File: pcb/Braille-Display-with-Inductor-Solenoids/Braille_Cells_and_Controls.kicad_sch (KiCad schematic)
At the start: 6 parts, among them U26 74HC595, U27 74HC595, U28 74HC595, U29 74HC595, U30 74HC595, U31 74HC595

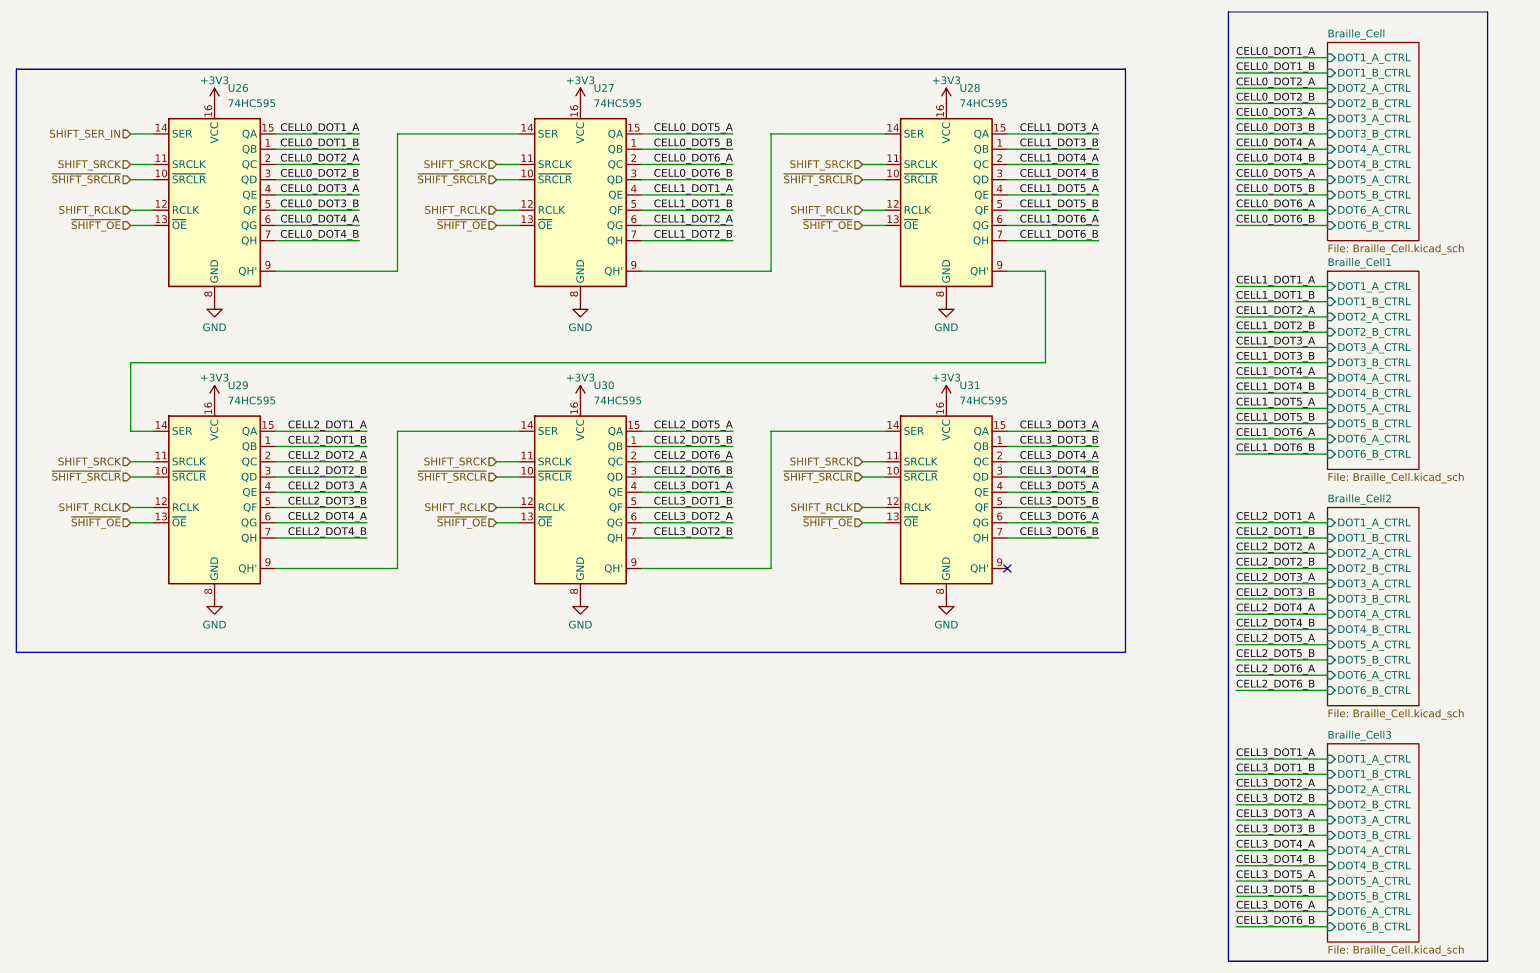
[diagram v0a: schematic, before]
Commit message: PCB (Rev 3): Switch to 2 inductors per cell (#2)
* WIP (Rev3): Switch to 2 inductors per cell

* WIP: Route one cell

* WIP: Route more of the board

* WIP: Swap around power input placement

* Finish and polish design

* Bit of tiny routing, export production file
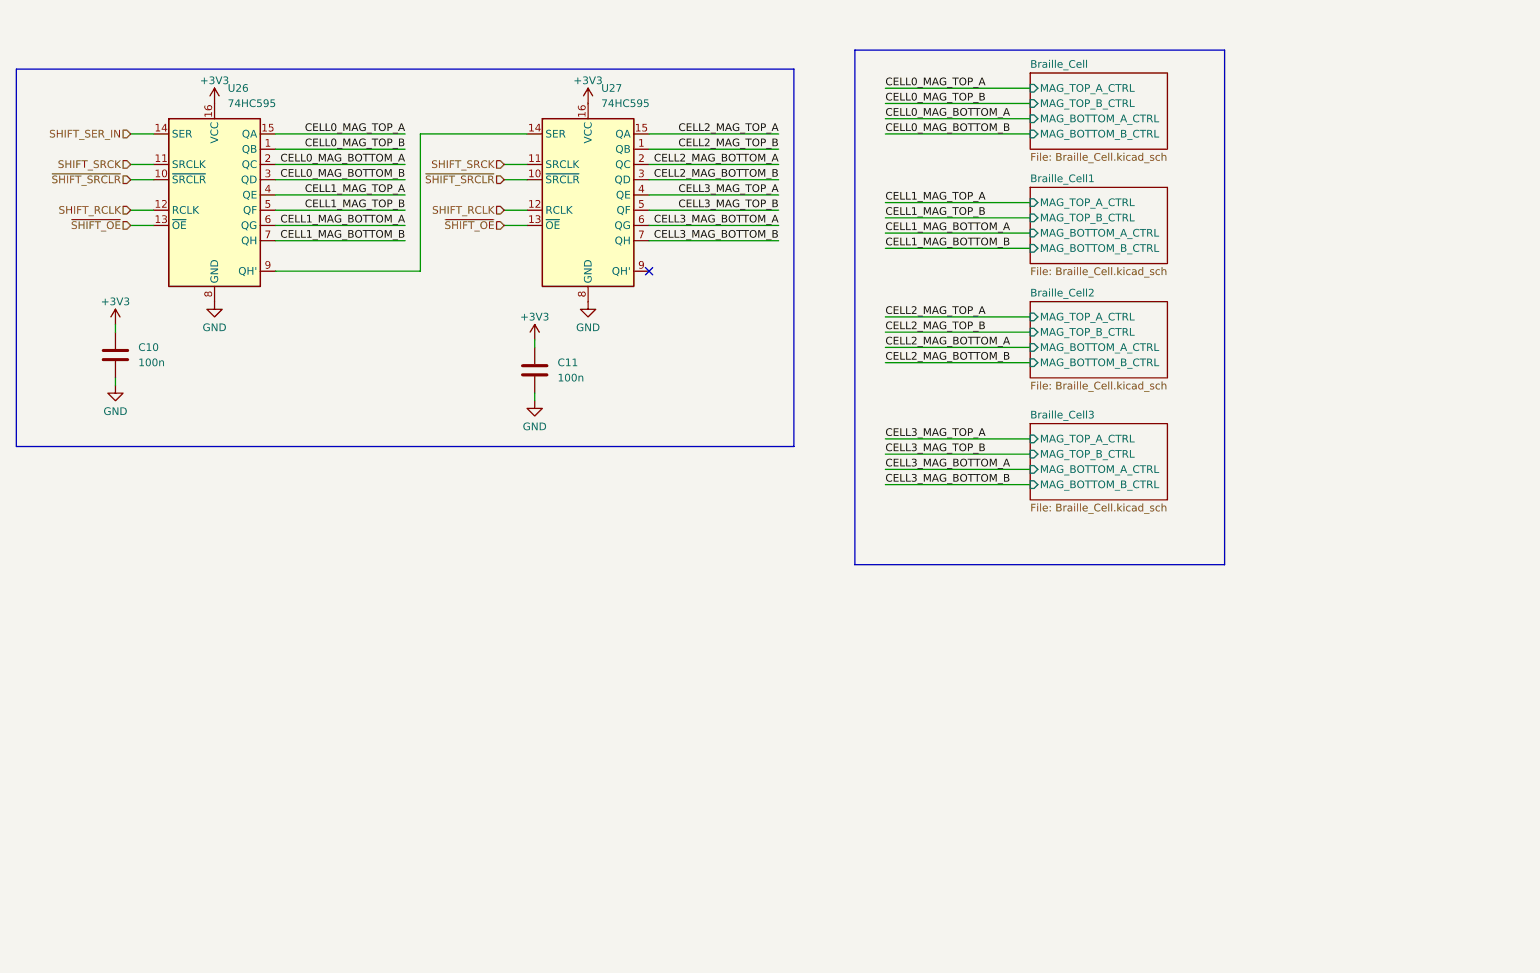
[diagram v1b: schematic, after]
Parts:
- removed U28, U29, U30, U31: 74HC595, Package_SO:SOP-16_3.9x9.9mm_P1.27mm, symbol 74xx:74HC595
- added C10, C11: 100n, Capacitor_SMD:C_1206_3216Metric_Pad1.33x1.80mm_HandSolder, symbol Device:C
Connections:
- net +3V3: now also C10.1, C11.1
- net GND: now also C10.2, C11.2
- net CELL0_DOT1_A renamed CELL0_MAG_TOP_A
- net CELL0_DOT1_B renamed CELL0_MAG_TOP_B
- net CELL0_DOT2_A renamed CELL0_MAG_BOTTOM_A
- net CELL0_DOT2_B renamed CELL0_MAG_BOTTOM_B
- net CELL0_DOT3_A renamed CELL1_MAG_TOP_A
- net CELL0_DOT3_B renamed CELL1_MAG_TOP_B
- net CELL0_DOT4_A renamed CELL1_MAG_BOTTOM_A
- net CELL0_DOT4_B renamed CELL1_MAG_BOTTOM_B
- net CELL0_DOT5_A renamed CELL2_MAG_TOP_A
- net CELL0_DOT5_B renamed CELL2_MAG_TOP_B
- net CELL0_DOT6_A renamed CELL2_MAG_BOTTOM_A
- net CELL0_DOT6_B renamed CELL2_MAG_BOTTOM_B
- net CELL1_DOT1_A renamed CELL3_MAG_TOP_A
- net CELL1_DOT1_B renamed CELL3_MAG_TOP_B
- net CELL1_DOT2_A renamed CELL3_MAG_BOTTOM_A
- net CELL1_DOT2_B renamed CELL3_MAG_BOTTOM_B
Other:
- sheet Braille_Cell ports: added MAG_BOTTOM_A_CTRL, MAG_BOTTOM_B_CTRL, MAG_TOP_A_CTRL, MAG_TOP_B_CTRL; removed DOT1_A_CTRL, DOT1_B_CTRL, DOT2_A_CTRL, DOT2_B_CTRL, DOT3_A_CTRL, DOT3_B_CTRL, DOT4_A_CTRL, DOT4_B_CTRL, DOT5_A_CTRL, DOT5_B_CTRL, DOT6_A_CTRL, DOT6_B_CTRL
- sheet Braille_Cell1 ports: added MAG_BOTTOM_A_CTRL, MAG_BOTTOM_B_CTRL, MAG_TOP_A_CTRL, MAG_TOP_B_CTRL; removed DOT1_A_CTRL, DOT1_B_CTRL, DOT2_A_CTRL, DOT2_B_CTRL, DOT3_A_CTRL, DOT3_B_CTRL, DOT4_A_CTRL, DOT4_B_CTRL, DOT5_A_CTRL, DOT5_B_CTRL, DOT6_A_CTRL, DOT6_B_CTRL
- sheet Braille_Cell2 ports: added MAG_BOTTOM_A_CTRL, MAG_BOTTOM_B_CTRL, MAG_TOP_A_CTRL, MAG_TOP_B_CTRL; removed DOT1_A_CTRL, DOT1_B_CTRL, DOT2_A_CTRL, DOT2_B_CTRL, DOT3_A_CTRL, DOT3_B_CTRL, DOT4_A_CTRL, DOT4_B_CTRL, DOT5_A_CTRL, DOT5_B_CTRL, DOT6_A_CTRL, DOT6_B_CTRL
- sheet Braille_Cell3 ports: added MAG_BOTTOM_A_CTRL, MAG_BOTTOM_B_CTRL, MAG_TOP_A_CTRL, MAG_TOP_B_CTRL; removed DOT1_A_CTRL, DOT1_B_CTRL, DOT2_A_CTRL, DOT2_B_CTRL, DOT3_A_CTRL, DOT3_B_CTRL, DOT4_A_CTRL, DOT4_B_CTRL, DOT5_A_CTRL, DOT5_B_CTRL, DOT6_A_CTRL, DOT6_B_CTRL
- moved on the sheet: U27

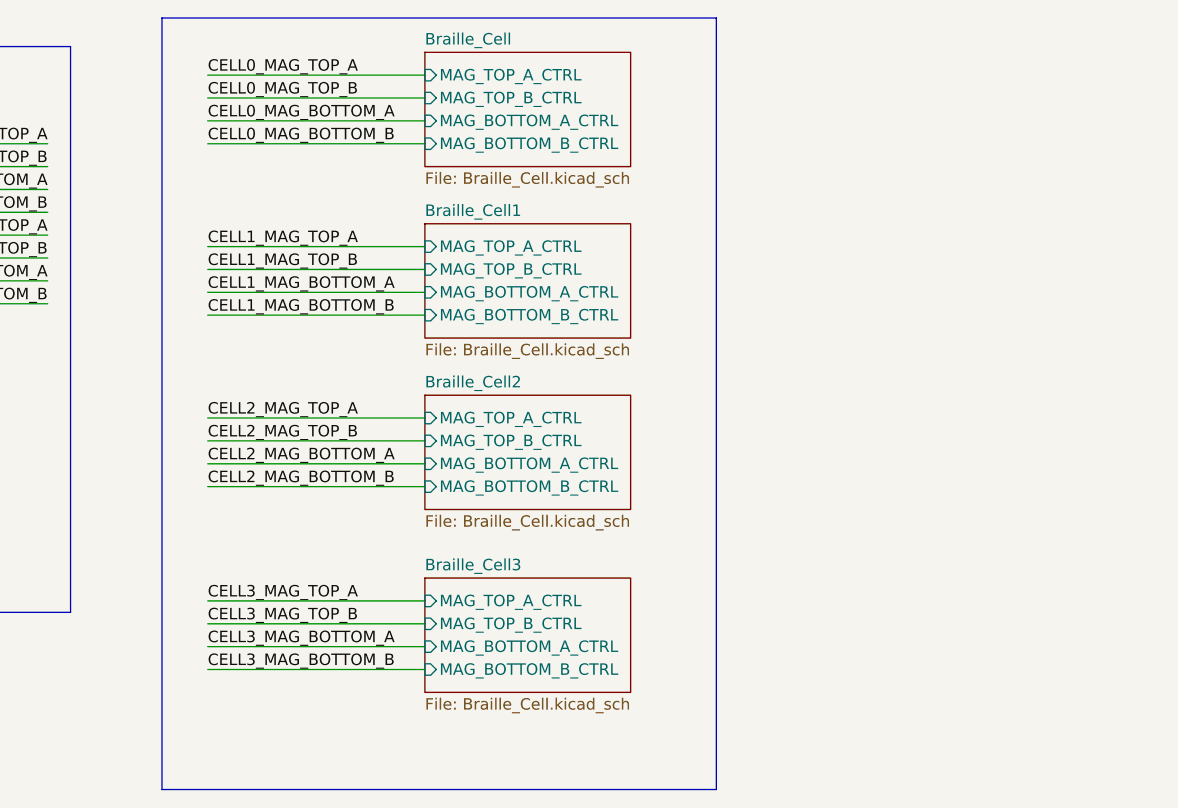
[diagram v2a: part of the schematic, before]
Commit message: pcb: WIP - Switch to new parts, layout
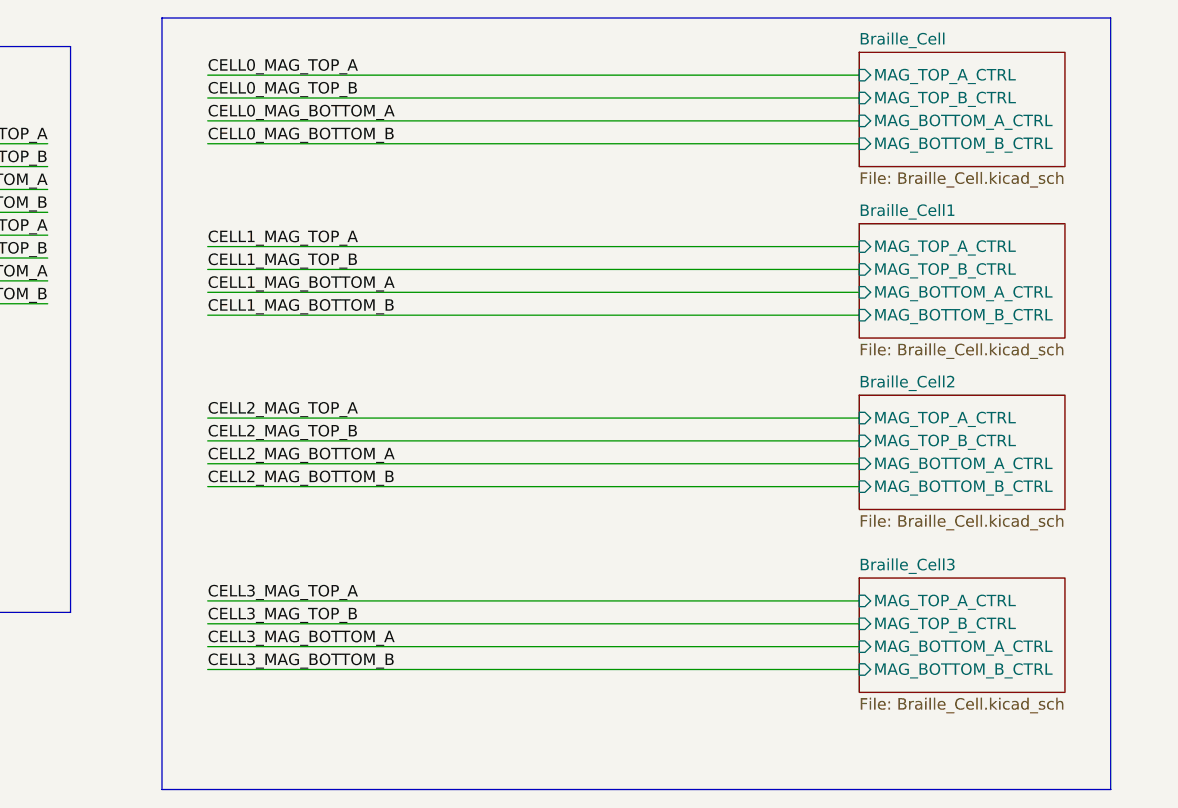
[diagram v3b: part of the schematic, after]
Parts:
- C10, C11: footprint Capacitor_SMD:C_1206_3216Metric_Pad1.33x1.80mm_HandSolder -> Capacitor_SMD:C_0603_1608Metric_Pad1.08x0.95mm_HandSolder
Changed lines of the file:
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@@
 	(rectangle
 		(start 160.02 19.05)
-		(end 221.615 104.775)
+		(end 265.43 104.775)
 		(stroke
 			(width 0)
@@
 	(wire
 		(pts
-			(xy 165.1 88.9) (xy 189.23 88.9)
+			(xy 165.1 88.9) (xy 237.49 88.9)
 		)
 		(stroke
@@
 	(wire
 		(pts
-			(xy 165.1 30.48) (xy 189.23 30.48)
+			(xy 165.1 30.48) (xy 237.49 30.48)
 		)
 		(stroke
@@
 	(wire
 		(pts
-			(xy 165.1 91.44) (xy 189.23 91.44)
-		)
-		(stroke
-			(width 0)
-			(type default)
-		)
-	)
-	(wire
-		(pts
-			(xy 165.1 66.04) (xy 189.23 66.04)
-		)
-		(stroke
-			(width 0)
-			(type default)
-		)
-	)
-	(wire
-		(pts
-			(xy 165.1 44.45) (xy 189.23 44.45)
+			(xy 165.1 91.44) (xy 237.49 91.44)
+		)
+		(stroke
+			(width 0)
+			(type default)
+		)
+	)
+	(wire
+		(pts
+			(xy 165.1 66.04) (xy 237.49 66.04)
+		)
+		(stroke
+			(width 0)
+			(type default)
+		)
+	)
+	(wire
+		(pts
+			(xy 165.1 44.45) (xy 237.49 44.45)
 		)
 		(stroke
@@
 	(wire
 		(pts
-			(xy 165.1 86.36) (xy 189.23 86.36)
+			(xy 165.1 86.36) (xy 237.49 86.36)
 		)
 		(stroke
@@
 	(wire
 		(pts
-			(xy 165.1 83.82) (xy 189.23 83.82)
+			(xy 165.1 83.82) (xy 237.49 83.82)
 		)
 		(stroke
@@
 	(wire
 		(pts
-			(xy 165.1 46.99) (xy 189.23 46.99)
-		)
-		(stroke
-			(width 0)
-			(type default)
-		)
-	)
-	(wire
-		(pts
-			(xy 165.1 33.02) (xy 189.23 33.02)
+			(xy 165.1 46.99) (xy 237.49 46.99)
+		)
+		(stroke
+			(width 0)
+			(type default)
+		)
+	)
+	(wire
+		(pts
+			(xy 165.1 33.02) (xy 237.49 33.02)
 		)
 		(stroke
@@
 	(wire
 		(pts
-			(xy 165.1 63.5) (xy 189.23 63.5)
+			(xy 165.1 63.5) (xy 237.49 63.5)
 		)
 		(stroke
@@
 	(wire
 		(pts
-			(xy 165.1 49.53) (xy 189.23 49.53)
+			(xy 165.1 49.53) (xy 237.49 49.53)
 		)
 		(stroke
@@
 	(wire
 		(pts
-			(xy 165.1 25.4) (xy 189.23 25.4)
+			(xy 165.1 25.4) (xy 237.49 25.4)
 		)
 		(stroke
@@
 	(wire
 		(pts
-			(xy 165.1 71.12) (xy 189.23 71.12)
+			(xy 165.1 71.12) (xy 237.49 71.12)
 		)
 		(stroke
@@
 	(wire
 		(pts
-			(xy 165.1 52.07) (xy 189.23 52.07)
+			(xy 165.1 52.07) (xy 237.49 52.07)
 		)
 		(stroke
@@
 	(wire
 		(pts
-			(xy 165.1 68.58) (xy 189.23 68.58)
+			(xy 165.1 68.58) (xy 237.49 68.58)
 		)
 		(stroke
@@
 	(wire
 		(pts
-			(xy 165.1 27.94) (xy 189.23 27.94)
+			(xy 165.1 27.94) (xy 237.49 27.94)
 		)
 		(stroke
@@
 			)
 		)
-		(property "Footprint" "Capacitor_SMD:C_1206_3216Metric_Pad1.33x1.80mm_HandSolder"
+		(property "Footprint" "Capacitor_SMD:C_0603_1608Metric_Pad1.08x0.95mm_HandSolder"
 			(at 37.7952 73.66 0)
 			(effects
@@
 			)
 		)
-		(property "Footprint" "Capacitor_SMD:C_1206_3216Metric_Pad1.33x1.80mm_HandSolder"
+		(property "Footprint" "Capacitor_SMD:C_0603_1608Metric_Pad1.08x0.95mm_HandSolder"
 			(at 107.6452 76.2 0)
 			(effects
@@
 	)
 	(sheet
-		(at 189.23 41.91)
+		(at 237.49 41.91)
 		(size 22.86 12.7)
 		(exclude_from_sim no)
@@
 		)
 		(property "Sheetname" "Braille_Cell1"
-			(at 189.23 41.1984 0)
+			(at 237.49 41.1984 0)
 			(effects
 				(font
@@
 		)
 		(property "Sheetfile" "Braille_Cell.kicad_sch"
-			(at 189.23 55.1946 0)
+			(at 237.49 55.1946 0)
 			(effects
 				(font
@@
 		)
 		(pin "MAG_BOTTOM_A_CTRL" input
-			(at 189.23 49.53 180)
+			(at 237.49 49.53 180)
 			(effects
 				(font
@@
 		)
 		(pin "MAG_BOTTOM_B_CTRL" input
-			(at 189.23 52.07 180)
+			(at 237.49 52.07 180)
 			(effects
 				(font
@@
 		)
 		(pin "MAG_TOP_A_CTRL" input
-			(at 189.23 44.45 180)
+			(at 237.49 44.45 180)
 			(effects
 				(font
@@
 		)
 		(pin "MAG_TOP_B_CTRL" input
-			(at 189.23 46.99 180)
+			(at 237.49 46.99 180)
 			(effects
 				(font
@@
 	)
 	(sheet
-		(at 189.23 81.28)
+		(at 237.49 81.28)
 		(size 22.86 12.7)
 		(exclude_from_sim no)
@@
 		)
 		(property "Sheetname" "Braille_Cell3"
-			(at 189.23 80.5684 0)
+			(at 237.49 80.5684 0)
 			(effects
 				(font
@@
 		)
 		(property "Sheetfile" "Braille_Cell.kicad_sch"
-			(at 189.23 94.5646 0)
+			(at 237.49 94.5646 0)
 			(effects
 				(font
@@
 		)
 		(pin "MAG_BOTTOM_A_CTRL" input
-			(at 189.23 88.9 180)
+			(at 237.49 88.9 180)
 			(effects
 				(font
@@
 		)
 		(pin "MAG_BOTTOM_B_CTRL" input
-			(at 189.23 91.44 180)
+			(at 237.49 91.44 180)
 			(effects
 				(font
@@
 		)
 		(pin "MAG_TOP_A_CTRL" input
-			(at 189.23 83.82 180)
+			(at 237.49 83.82 180)
 			(effects
 				(font
@@
 		)
 		(pin "MAG_TOP_B_CTRL" input
-			(at 189.23 86.36 180)
+			(at 237.49 86.36 180)
 			(effects
 				(font
@@
 	)
 	(sheet
-		(at 189.23 60.96)
+		(at 237.49 60.96)
 		(size 22.86 12.7)
 		(exclude_from_sim no)
@@
 		)
 		(property "Sheetname" "Braille_Cell2"
-			(at 189.23 60.2484 0)
+			(at 237.49 60.2484 0)
 			(effects
 				(font
@@
 		)
 		(property "Sheetfile" "Braille_Cell.kicad_sch"
-			(at 189.23 74.2446 0)
+			(at 237.49 74.2446 0)
 			(effects
 				(font
@@
 		)
 		(pin "MAG_BOTTOM_A_CTRL" input
-			(at 189.23 68.58 180)
+			(at 237.49 68.58 180)
 			(effects
 				(font
@@
 		)
 		(pin "MAG_BOTTOM_B_CTRL" input
-			(at 189.23 71.12 180)
+			(at 237.49 71.12 180)
 			(effects
 				(font
@@
 		)
 		(pin "MAG_TOP_A_CTRL" input
-			(at 189.23 63.5 180)
+			(at 237.49 63.5 180)
 			(effects
 				(font
@@
 		)
 		(pin "MAG_TOP_B_CTRL" input
-			(at 189.23 66.04 180)
+			(at 237.49 66.04 180)
 			(effects
 				(font
@@
 	)
 	(sheet
-		(at 189.23 22.86)
+		(at 237.49 22.86)
 		(size 22.86 12.7)
 		(exclude_from_sim no)
@@
 		)
 		(property "Sheetname" "Braille_Cell"
-			(at 189.23 22.1484 0)
+			(at 237.49 22.1484 0)
 			(effects
 				(font
@@
 		)
 		(property "Sheetfile" "Braille_Cell.kicad_sch"
-			(at 189.23 36.1446 0)
+			(at 237.49 36.1446 0)
 			(effects
 				(font
@@
 		)
 		(pin "MAG_BOTTOM_A_CTRL" input
-			(at 189.23 30.48 180)
+			(at 237.49 30.48 180)
 			(effects
 				(font
@@
 		)
 		(pin "MAG_BOTTOM_B_CTRL" input
-			(at 189.23 33.02 180)
+			(at 237.49 33.02 180)
 			(effects
 				(font
@@
 		)
 		(pin "MAG_TOP_A_CTRL" input
-			(at 189.23 25.4 180)
+			(at 237.49 25.4 180)
 			(effects
 				(font
@@
 		)
 		(pin "MAG_TOP_B_CTRL" input
-			(at 189.23 27.94 180)
-			(effects
-				(font
+			(at 237.49 27.94 180)
+			(effects
+				(font
